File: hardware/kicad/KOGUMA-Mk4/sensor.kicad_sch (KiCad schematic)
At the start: 40 parts, among them J5 ENC_L, J6 ENC_R, U70 NJU6080, U71 NJU6080, U72 NJU6080, U73 NJU6080, U74 AD8606ARM, U75 AD8606ARM, U76 LSM6DSR

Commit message: 受光のアンプを OPA2354(帰還 0.5pF)に、エンコーダを MT6835 にする
- 割り込みの周期を極限まで速くしたときのネックを減らすため。受光の回路が一番遅かった
  (AD8606 + 820k ∥ 2.2pF で 1% まで 約8µs)。OPA2354(100MHz)+ 0.5pF C0G で 約1.9µs
- 発光の定電流 IC は NJU6080 のまま(ON の遅れ 2.5µs。NCR321PAS は PWM 10kHz までで、
  OPV332 には 3.3V で電圧の余裕が足りない)
- エンコーダ: MT6835(ノイズ 0.0015° rms、遅れ 約10µs、SPI モード3)。校正用の CAL_EN は
  エンコーダの基板のはんだジャンパにし、メイン基板への線は6本のまま
- オペアンプの電源に 100nF を足す

Co-Authored-By: Claude Opus 5.5 <noreply@anthropic.com>
Claude-Session: https://claude.ai/code/session_01H2Zvpqxqu2v63zaiCMmfT3
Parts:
- removed U74, U75: AD8606ARM, Package_SO:MSOP-8_3x3mm_P0.65mm, symbol Amplifier_Operational:AD8606ARM
- added C83, C84: 100n, Capacitor_SMD:C_0603_1608Metric, symbol Device:C
- added U74, U75: OPA2354, Package_SO:VSSOP-8_3x3mm_P0.65mm, symbol KOGUMA-Mk4:OPA2354
- C74, C75, C76, C77: value 2.2p -> 0.5p C0G
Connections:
- net +3V3: now also C83.1, C84.1, U74.8 (V+), U75.8 (V+)
- net GND: now also C83.2, C84.2, U74.4 (V-), U75.4 (V-)
- net PD_BIAS: now also U74.3 (+), U74.5 (+), U75.3 (+), U75.5 (+)
- net WALL_FL: now also U74.1
- net WALL_FR: now also U75.1
- net WALL_L: now also U75.7
- net WALL_R: now also U74.7
- net at C74.1, D74.1 (K), R74.1: now also U74.2 (-)
- net at C77.1, D77.1 (K), R77.1: now also U75.6 (-)
- net at C75.1, D75.1 (K), R75.1: now also U74.6 (-)
- net at C76.1, D76.1 (K), R76.1: now also U75.2 (-)
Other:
- note added: "OPA2354 の電源(100nF + 10µF をすぐそばに)と PD_BIAS(MK3 と同じ)"
- note added: "エンコーダ: MT6835(TSSOP-16、SPI モード3、最高 約16MHz)を小さな基板(ToraNeko.Mk3 と同じ形)に載せ、6本の線でつなぐ。 パスコンと、校正用の CAL_EN を VDD につなぐはんだジャンパはエンコーダの基板に置く。ピンの並びは基板を描くときに合わせる(仮)。"
- note added: "受光: SFH 229 FA を OPA2354(100MHz)で電流-電圧変換(820kΩ ∥ 0.5pF C0G、帯域 約390kHz、1% まで 約1.9µs)。+ 入力に PD_BIAS(約0.148V)。MK3 は AD8606 + 2.2pF で 約8µs。 0.5pF は浮遊容量が効くので実機で波形を見て決める。アンプとフォトダイオードはモーター・SMPS の電流の通り道から離し、GND は1点でつなぐ。"
- note removed: "AD8606 の電源(10µF)と PD_BIAS(MK3 と同じ)"
- note removed: "エンコーダ: AS5047P は小さな基板(ToraNeko.Mk3 と同じ形)に載せ、6本の線でつなぐ。AS5047P のパスコンはその基板に置く。 ピンの並びはエンコーダの基板を描くときに合わせる(仮)。"
- note removed: "受光: SFH 229 FA を AD8606 で電流-電圧変換(820kΩ ∥ 2.2pF)。+ 入力に PD_BIAS(3.3V × 47 / 1047 = 約0.148V)。MK3 と同じ。 アンプとフォトダイオードはモーター・SMPS の電流の通り道から離し、GND は1点でつなぐ(MK3 は FL・L にノイズがのった)。"

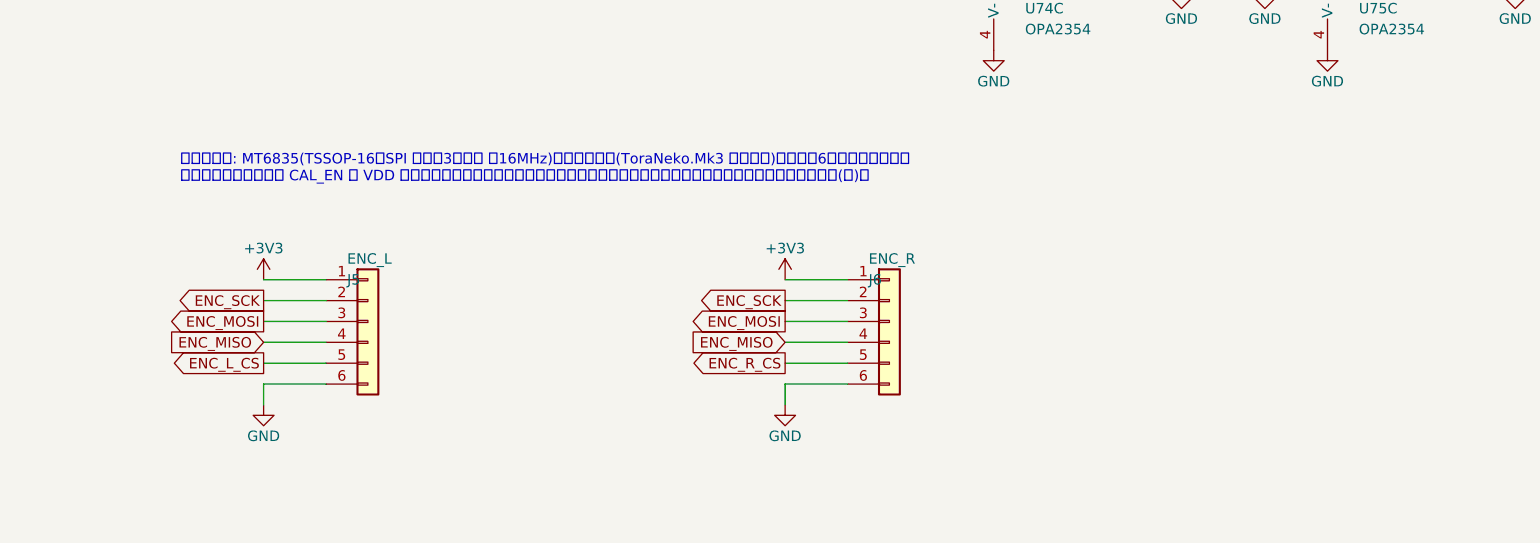
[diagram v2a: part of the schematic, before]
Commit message: エンコーダの基板を作る(MT6835、メイン基板の穴に通してはんだ付け)
- hardware/kicad/KOGUMA-Mk4_Encoder: 回路図と基板(6 x 12.8 x 0.6mm、2層)。
  MT6835 の中心は下の辺から 4.5mm、部品はすべてチップの面。DRC・ERC エラー 0
- 線をやめ、メイン基板の穴(ENC_Base_Slot、NPTH 1.0 x 6.6mm)に通して
  上の面でパッド7つをはんだ付けする。マウントの上とメイン基板の間に線を
  通すすき間がないため
- CAL_EN ははんだジャンパをやめて MCU の PC15(ENC_CAL、左右共通)へ。
  ジャンパはメイン基板の下に隠れて触れないため
- J5・J6 を7ピンに、pinmap(使う44本、残り2本)・spec・bom・mount を更新

Co-Authored-By: Claude Opus 5.5 <noreply@anthropic.com>
Claude-Session: https://claude.ai/code/session_01H2Zvpqxqu2v63zaiCMmfT3
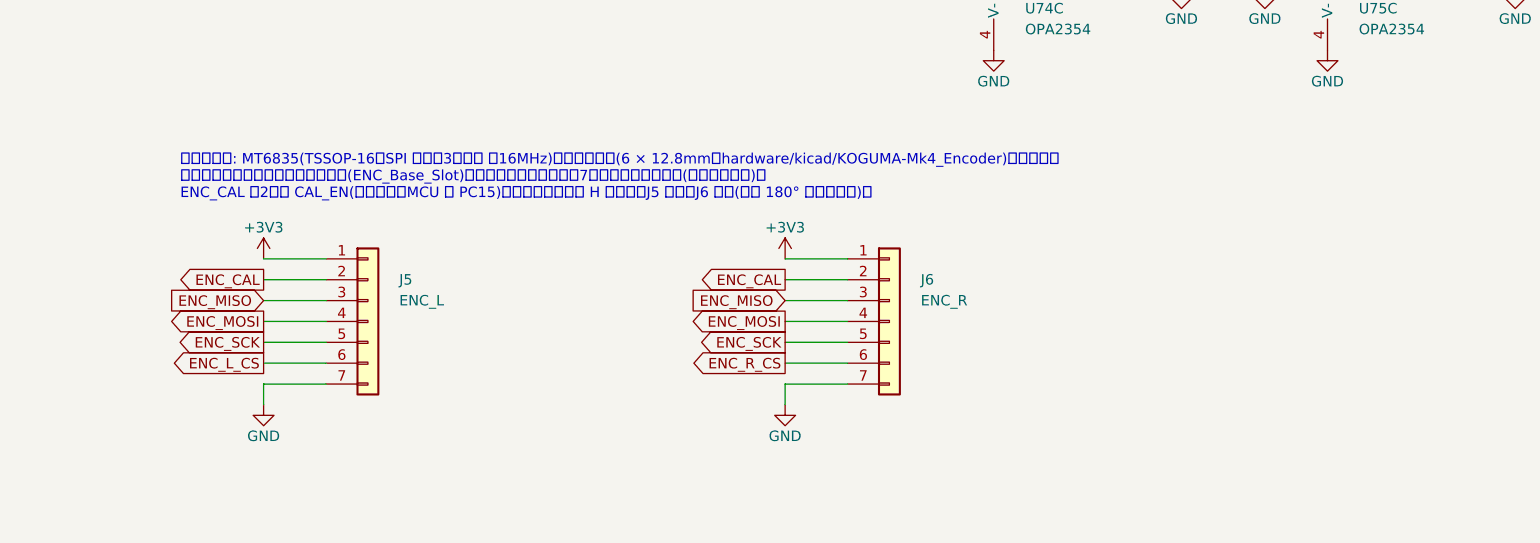
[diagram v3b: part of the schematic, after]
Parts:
- removed J5: ENC_L, Connector_Wire:SolderWire-0.127sqmm_1x06_P3.7mm_D0.48mm_OD1mm, symbol Connector_Generic:Conn_01x06
- removed J6: ENC_R, Connector_Wire:SolderWire-0.127sqmm_1x06_P3.7mm_D0.48mm_OD1mm, symbol Connector_Generic:Conn_01x06
- added J5: ENC_L, KOGUMA-Mk4:ENC_Base_Slot, symbol Connector_Generic:Conn_01x07
- added J6: ENC_R, KOGUMA-Mk4:ENC_Base_Slot, symbol Connector_Generic:Conn_01x07
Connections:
- net +3V3: now also J5.1 (Pin_1), J6.1 (Pin_1)
- net ENC_L_CS: now also J5.6 (Pin_6)
- net ENC_MISO: now also J5.3 (Pin_3), J6.3 (Pin_3)
- net ENC_MOSI: now also J5.4 (Pin_4), J6.4 (Pin_4)
- net ENC_R_CS: now also J6.6 (Pin_6)
- net ENC_SCK: now also J5.5 (Pin_5), J6.5 (Pin_5)
- net GND: now also J5.7 (Pin_7), J6.7 (Pin_7)
- new net ENC_CAL: J5.2 (Pin_2), J6.2 (Pin_2)
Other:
- note added: "エンコーダ: MT6835(TSSOP-16、SPI モード3、最高 約16MHz)を小さな基板(6 × 12.8mm、hardware/kicad/KOGUMA-Mk4_Encoder)に載せる。 エンコーダの基板はメイン基板の穴(ENC_Base_Slot)を通し、上の面でパッド7つをはんだ付けする(線は使わない)。 ENC_CAL は2個の CAL_EN(左右共通、MCU の PC15)。校正のときだけ H にする。J5 は左、J6 は右(右は 180° 回して置く)。"
- note removed: "エンコーダ: MT6835(TSSOP-16、SPI モード3、最高 約16MHz)を小さな基板(ToraNeko.Mk3 と同じ形)に載せ、6本の線でつなぐ。 パスコンと、校正用の CAL_EN を VDD につなぐはんだジャンパはエンコーダの基板に置く。ピンの並びは基板を描くときに合わせる(仮)。"
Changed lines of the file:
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@@
 	)
 	(symbol
-		(lib_id "Connector_Generic:Conn_01x06")
+		(lib_id "Connector_Generic:Conn_01x07")
 		(at 220.98 231.14 0)
 		(unit 1)
@@
 		(dnp no)
 		(property "Reference" "J5"
-			(at 218.44 226.06 0)
+			(at 224.79 226.06 0)
 			(effects
 				(font
@@
 		)
 		(property "Value" "ENC_L"
-			(at 218.44 223.52 0)
+			(at 224.79 228.6 0)
 			(effects
 				(font
@@
 			)
 		)
-		(property "Footprint" "Connector_Wire:SolderWire-0.127sqmm_1x06_P3.7mm_D0.48mm_OD1mm"
+		(property "Footprint" "KOGUMA-Mk4:ENC_Base_Slot"
 			(at 220.98 231.14 0)
 			(effects
@@
 		)
 		(pin "6"
+		)
+		(pin "7"
 		)
 		(instances
@@
 	(wire
 		(pts
-			(xy 208.28 226.06) (xy 215.9 226.06)
+			(xy 208.28 223.52) (xy 215.9 223.52)
 		)
 		(stroke
@@
 	(symbol
 		(lib_id "power:+3V3")
-		(at 208.28 226.06 0)
+		(at 208.28 223.52 0)
 		(unit 1)
 		(exclude_from_sim no)
@@
 		(dnp no)
 		(property "Reference" "#PWR37"
-			(at 208.28 228.6 0)
+			(at 208.28 226.06 0)
 			(effects
 				(font
@@
 		)
 		(property "Value" "+3V3"
-			(at 208.28 222.25 0)
+			(at 208.28 219.71 0)
 			(effects
 				(font
@@
 		)
 		(property "Footprint" ""
-			(at 208.28 226.06 0)
+			(at 208.28 223.52 0)
 			(effects
 				(font
@@
 		)
 		(property "Datasheet" "~"
-			(at 208.28 226.06 0)
+			(at 208.28 223.52 0)
 			(effects
 				(font
@@
 		)
 		(property "Description" ""
-			(at 208.28 226.06 0)
+			(at 208.28 223.52 0)
 			(effects
 				(font
@@
 	(wire
 		(pts
+			(xy 208.28 226.06) (xy 215.9 226.06)
+		)
+		(stroke
+			(width 0)
+			(type default)
+		)
+	)
+	(global_label "ENC_CAL"
+		(shape output)
+		(at 208.28 226.06 180)
+		(fields_autoplaced yes)
+		(effects
+			(font
+				(size 1.27 1.27)
+			)
+			(justify right)
+		)
+		(property "Intersheetrefs" "${INTERSHEET_REFS}"
+			(at 208.28 226.06 0)
+			(effects
+				(font
+					(size 1.27 1.27)
+				)
+				(hide yes)
+			)
+		)
+	)
+	(wire
+		(pts
 			(xy 208.28 228.6) (xy 215.9 228.6)
 		)
@@
 		)
 	)
-	(global_label "ENC_SCK"
-		(shape output)
+	(global_label "ENC_MISO"
+		(shape input)
 		(at 208.28 228.6 180)
 		(fields_autoplaced yes)
@@
 		)
 	)
-	(global_label "ENC_MISO"
-		(shape input)
+	(global_label "ENC_SCK"
+		(shape output)
 		(at 208.28 233.68 180)
 		(fields_autoplaced yes)
@@
 	)
 	(symbol
-		(lib_id "Connector_Generic:Conn_01x06")
+		(lib_id "Connector_Generic:Conn_01x07")
 		(at 284.48 231.14 0)
 		(unit 1)
@@
 		(dnp no)
 		(property "Reference" "J6"
-			(at 281.94 226.06 0)
+			(at 288.29 226.06 0)
 			(effects
 				(font
@@
 		)
 		(property "Value" "ENC_R"
-			(at 281.94 223.52 0)
+			(at 288.29 228.6 0)
 			(effects
 				(font
@@
 			)
 		)
-		(property "Footprint" "Connector_Wire:SolderWire-0.127sqmm_1x06_P3.7mm_D0.48mm_OD1mm"
+		(property "Footprint" "KOGUMA-Mk4:ENC_Base_Slot"
 			(at 284.48 231.14 0)
 			(effects
@@
 		)
 		(pin "6"
+		)
+		(pin "7"
 		)
 		(instances
@@
 	(wire
 		(pts
-			(xy 271.78 226.06) (xy 279.4 226.06)
+			(xy 271.78 223.52) (xy 279.4 223.52)
 		)
 		(stroke
@@
 	(symbol
 		(lib_id "power:+3V3")
-		(at 271.78 226.06 0)
+		(at 271.78 223.52 0)
 		(unit 1)
 		(exclude_from_sim no)
@@
 		(dnp no)
 		(property "Reference" "#PWR39"
-			(at 271.78 228.6 0)
+			(at 271.78 226.06 0)
 			(effects
 				(font
@@
 		)
 		(property "Value" "+3V3"
-			(at 271.78 222.25 0)
+			(at 271.78 219.71 0)
 			(effects
 				(font
@@
 		)
 		(property "Footprint" ""
-			(at 271.78 226.06 0)
+			(at 271.78 223.52 0)
 			(effects
 				(font
@@
 		)
 		(property "Datasheet" "~"
-			(at 271.78 226.06 0)
+			(at 271.78 223.52 0)
 			(effects
 				(font
@@
 		)
 		(property "Description" ""
-			(at 271.78 226.06 0)
+			(at 271.78 223.52 0)
 			(effects
 				(font
@@
 	(wire
 		(pts
+			(xy 271.78 226.06) (xy 279.4 226.06)
+		)
+		(stroke
+			(width 0)
+			(type default)
+		)
+	)
+	(global_label "ENC_CAL"
+		(shape output)
+		(at 271.78 226.06 180)
+		(fields_autoplaced yes)
+		(effects
+			(font
+				(size 1.27 1.27)
+			)
+			(justify right)
+		)
+		(property "Intersheetrefs" "${INTERSHEET_REFS}"
+			(at 271.78 226.06 0)
+			(effects
+				(font
+					(size 1.27 1.27)
+				)
+				(hide yes)
+			)
+		)
+	)
+	(wire
+		(pts
 			(xy 271.78 228.6) (xy 279.4 228.6)
 		)
@@
 		)
 	)
-	(global_label "ENC_SCK"
-		(shape output)
+	(global_label "ENC_MISO"
+		(shape input)
 		(at 271.78 228.6 180)
 		(fields_autoplaced yes)
@@
 		)
 	)
-	(global_label "ENC_MISO"
-		(shape input)
+	(global_label "ENC_SCK"
+		(shape output)
 		(at 271.78 233.68 180)
 		(fields_autoplaced yes)
@@
 		)
 	)
-	(text "エンコーダ: MT6835(TSSOP-16、SPI モード3、最高 約16MHz)を小さな基板(ToraNeko.Mk3 と同じ形)に載せ、6本の線でつなぐ。\nパスコンと、校正用の CAL_EN を VDD につなぐはんだジャンパはエンコーダの基板に置く。ピンの並びは基板を描くときに合わせる(仮)。"
+	(text "エンコーダ: MT6835(TSSOP-16、SPI モード3、最高 約16MHz)を小さな基板(6 × 12.8mm、hardware/kicad/KOGUMA-Mk4_Encoder)に載せる。\nエンコーダの基板はメイン基板の穴(ENC_Base_Slot)を通し、上の面でパッド7つをはんだ付けする(線は使わない)。\nENC_CAL は2個の CAL_EN(左右共通、MCU の PC15)。校正のときだけ H にする。J5 は左、J6 は右(右は 180° 回して置く)。"
 		(exclude_from_sim no)
 		(at 198.12 210.82 0)
